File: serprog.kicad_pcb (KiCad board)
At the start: 2 copper layers, 53 x 23.5 mm, 44 parts, among them J1 USB_B_Micro, J2 Conn_01x04, SW1 SW_Push_SPDT, U1 TXS0108EPW, U2 XC6206PxxxMR1v8, U3 XC6206PxxxMR3v3, U4 AT25xxx, U5 STM32F102R8Tx, Y1 8M

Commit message: v0.1
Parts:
- removed J2: Conn_01x04, Connector_PinHeader_2.54mm:PinHeader_1x04_P2.54mm_Vertical
- removed TP1, TP2, TP3, TP4: TestPoint, TestPoint:TestPoint_Pad_D1.0mm
- added 3V3: TestPoint, TestPoint:TestPoint_Pad_D1.0mm, B.Cu at (119.4, 70.0)
- added G: TestPoint, TestPoint:TestPoint_Pad_D1.0mm, B.Cu at (121.9, 70.0)
- added REF**: KiCad-Logo2_5mm_SilkScreen, Symbol:KiCad-Logo2_5mm_SilkScreen, F.Cu at (146.0, 81.6)
- added RX: TestPoint, TestPoint:TestPoint_Pad_D1.0mm, B.Cu at (124.5, 70.0)
- added TX: TestPoint, TestPoint:TestPoint_Pad_D1.0mm, B.Cu at (127.0, 70.0)
- C10, C11, R10, R11, R12, R13, R8, U1: moved to F.Cu
- J1: footprint Connector_USB:USB_Micro-B_Molex_47346-0001 -> Connector_USB:USB_Micro-B_Molex-105017-0001
- moved C2 27.5 mm to (116.3, 81.5)
- moved R13 27.2 mm to (149.8, 62.4), turned to 270 degrees
- moved R11 25.9 mm to (151.8, 62.4), turned to 270 degrees
- moved R12 24.1 mm to (147.8, 62.4), turned to 270 degrees
- moved C14 21.8 mm to (115.6, 65.5), turned to 90 degrees
- moved R14 21.6 mm to (132.2, 81.5), turned to 270 degrees
- moved C12 20.7 mm to (133.0, 77.6), turned to 180 degrees
- moved SW1 20.0 mm to (133.8, 64.5), turned to 90 degrees
- moved Y1 19.9 mm to (120.8, 81.5), turned to 0 degrees
- moved R10 19.8 mm to (145.9, 62.4), turned to 270 degrees
- moved C3 18.5 mm to (130.1, 81.5), turned to 90 degrees
- moved D1 17.9 mm to (134.4, 81.4), turned to 90 degrees
- moved R8 17.4 mm to (137.8, 66.5), turned to 0 degrees
- moved C7 17.1 mm to (133.0, 75.8), turned to 180 degrees
- moved C8 14.6 mm to (130.5, 59.6), turned to 270 degrees
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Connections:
- SW1 pad : GND -> (no net)
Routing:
- net +3V3: track 165.0 -> 116.8 mm, vias 6 -> 5
- net +1V8: track 51.3 -> 15.3 mm, vias 1 -> 0
- net GND: track 78.1 -> 45.9 mm, vias 25 -> 36
- net BOOT0: track 33.7 -> 5.75 mm
- net PA0: track 35.1 -> 12.3 mm
- net FLASH_MISO: track 32.6 -> 17.1 mm
- net FLASH_SCK: track 41.4 -> 28.9 mm, vias 2 -> 1
- net BOOT1: track 18.5 -> 6.66 mm
- net nRST: track 28.7 -> 17.0 mm
- net FLASH_NSS: track 27.7 -> 17.7 mm, vias 0 -> 3
- net FLASH_VCC: track 55.7 -> 65.4 mm, vias 2 -> 3
- net USART1_TX: track 15.5 -> 7.17 mm
- net USART1_RX: track 13.0 -> 5.37 mm
- net PA13: track 4.60 -> 11.2 mm
- net USBDP: track 5.18 -> 11.6 mm
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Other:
- board size 53 x 23.5 mm -> 53 x 29.5 mm
- board text added: "0"
- board text added: "1"
- board text added: "3.3<- ->1.8"
- board text added: "STM32-vserprog"
- board text removed: "1.8 V 3.3"
- board text removed: "G V T R"

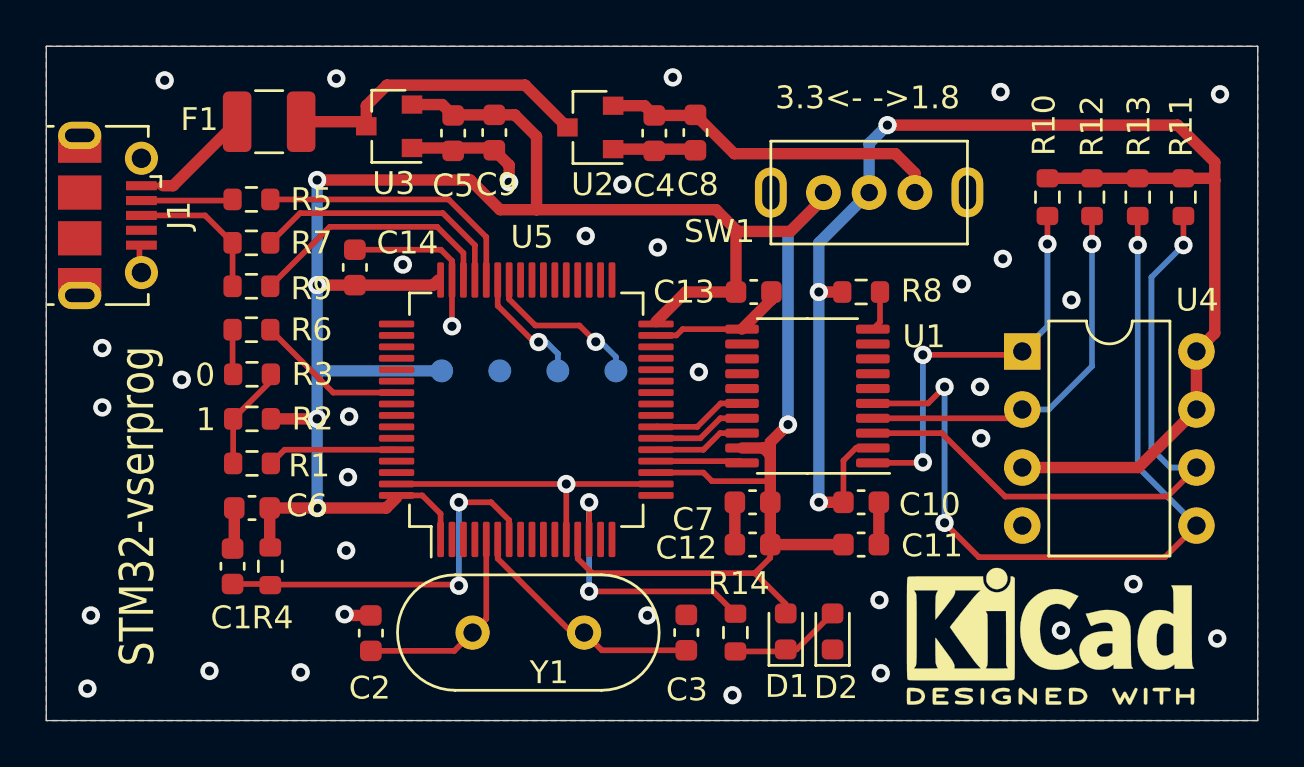
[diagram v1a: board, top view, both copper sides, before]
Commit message: delete useless testpad
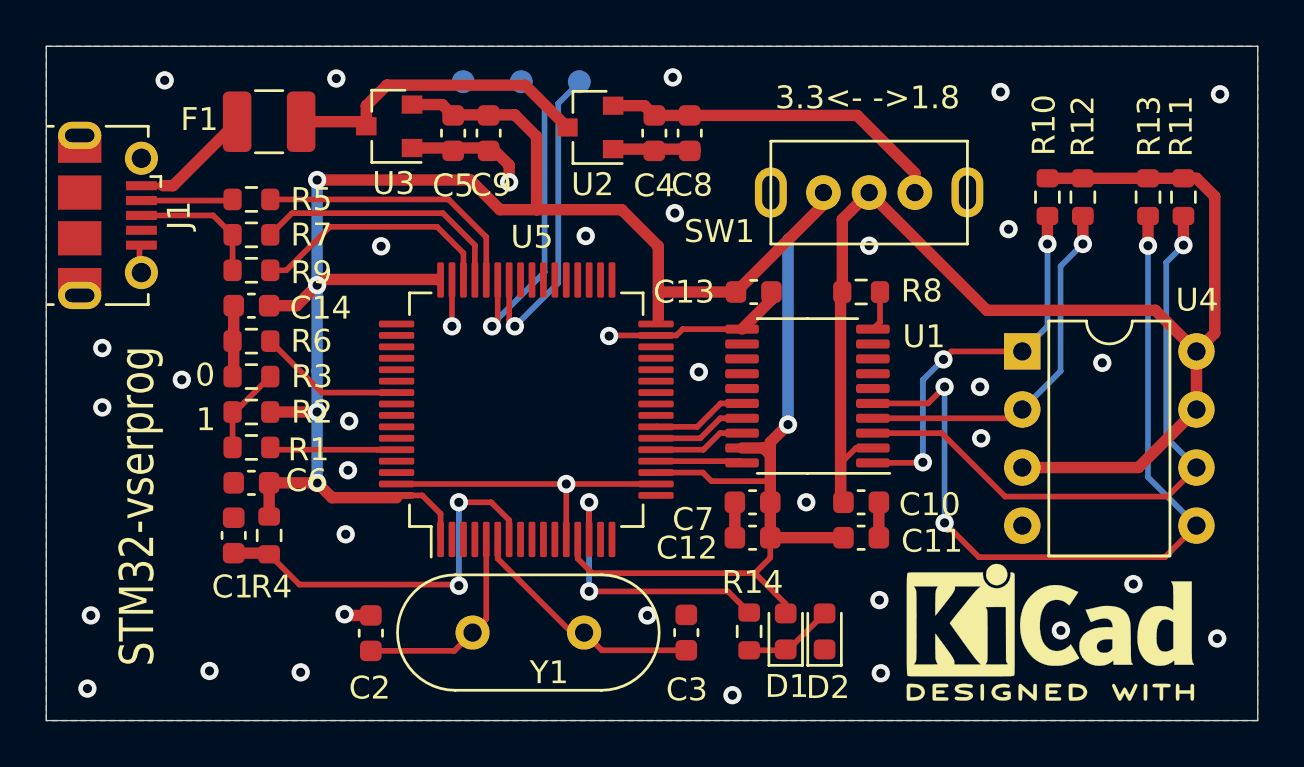
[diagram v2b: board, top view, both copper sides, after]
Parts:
- removed 3V3: TestPoint, TestPoint:TestPoint_Pad_D1.0mm
- G: value TestPoint -> GND
- RX: value TestPoint -> RX
- TX: value TestPoint -> TX
- moved RX 12.8 mm to (122.9, 57.4)
- moved G 12.8 mm to (120.3, 57.4)
- moved TX 12.8 mm to (125.4, 57.4)
- moved C14 4.83 mm to (111.1, 67.2), turned to 180 degrees
- moved R4 1.35 mm to (111.8, 77.2)
- moved C1 1.35 mm to (110.3, 77.2)
- moved C6 1.10 mm to (111.1, 74.9)
- moved R1 0.70 mm to (111.1, 73.3)
- moved R9 0.70 mm to (111.1, 65.6)
- moved R14 0.60 mm to (132.8, 81.4)
- moved R6 0.50 mm to (111.1, 68.7)
- moved R13 0.45 mm to (150.3, 62.4)
- moved R12 0.40 mm to (147.4, 62.4)
- moved R7 0.35 mm to (111.1, 64.0)
- moved D2 0.35 mm to (136.2, 81.4)
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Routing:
- net USART1_RX: track 5.37 -> 14.2 mm
- net USART1_TX: track 7.17 -> 14.0 mm
- net +3V3: track 116.8 -> 110.3 mm
- net FLASH_VCC: track 65.4 -> 60.6 mm, vias 3 -> 0
- net GND: track 45.9 -> 41.4 mm, vias 36 -> 37
- net FLASH_SCK: track 28.9 -> 27.7 mm
- net Net-(D1-Pad1): track 4.94 -> 3.97 mm
- net FLASH_MISO: track 17.1 -> 16.3 mm
- net Net-(R1-Pad1): track 4.58 -> 3.78 mm
- net FLASH_NSS: track 17.7 -> 17.0 mm
- net PA0: track 12.3 -> 12.9 mm

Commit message: v0.2
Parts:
- U1: value TXS0108EPW -> TXB0104PW; footprint Package_SO:TSSOP-20_4.4x6.5mm_P0.65mm -> Package_SO:TSSOP-14_4.4x5mm_P0.65mm
- moved C13 2.05 mm to (133.0, 68.6)
- moved R8 2.05 mm to (137.8, 68.6), turned to 180 degrees
- moved U1 1.08 mm to (135.4, 72.2)
- moved REF** 0.29 mm to (146.1, 81.7)
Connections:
- SW1 pad : (no net) -> GND
- U1 pad 1: FLASH_NSS -> FLASH_VCC
- U1 pad 10: Net-(R8-Pad2) -> SPI1_MOSI
- U1 pad 11: GND -> SPI1_MISO
- U1 pad 12: Net-(U1-Pad12) -> SPI1_SCK
- U1 pad 13: Net-(U1-Pad13) -> SPI1_NSS
- U1 pad 14: Net-(U1-Pad14) -> +3V3
- U1 pad 2: FLASH_VCC -> FLASH_NSS
- U1 pad 7: Net-(U1-Pad7) -> GND
- U1 pad 8: Net-(U1-Pad8) -> Net-(R8-Pad2)
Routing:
- net FLASH_VCC: track 60.6 -> 64.9 mm, vias 0 -> 1
- net GND: track 41.4 -> 37.8 mm, vias 37 -> 39
- net Net-(R8-Pad2): track 1.75 -> 5.09 mm
- net +3V3: track 110.3 -> 113.6 mm
- net FLASH_NSS: track 17.0 -> 18.0 mm
- net FLASH_MOSI: track 36.0 -> 35.2 mm
- net FLASH_MISO: track 16.3 -> 16.9 mm
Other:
- board text added: "3.3V 1.8V"
- board text added: "STM32-serprog"
- board text added: "https://github.com/liweihao-cn/stm32-serprog"
- board text removed: "3.3<- ->1.8"
- board text removed: "STM32-vserprog"

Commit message: fix url issue
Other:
- board text added: "https://github.com/ieiao/stm32-serprog"
- board text removed: "https://github.com/liweihao-cn/stm32-serprog"
